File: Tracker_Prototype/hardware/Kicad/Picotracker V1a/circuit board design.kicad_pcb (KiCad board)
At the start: 2 copper layers, 31 x 20.1 mm, 27 parts, among them J1 Conn_01x06, J2 GND, J3 3.3V, J4 Unconnected, U1 MAX-M8C, U3 CMWX1ZZABZ-078, U6 MS5607-02BA

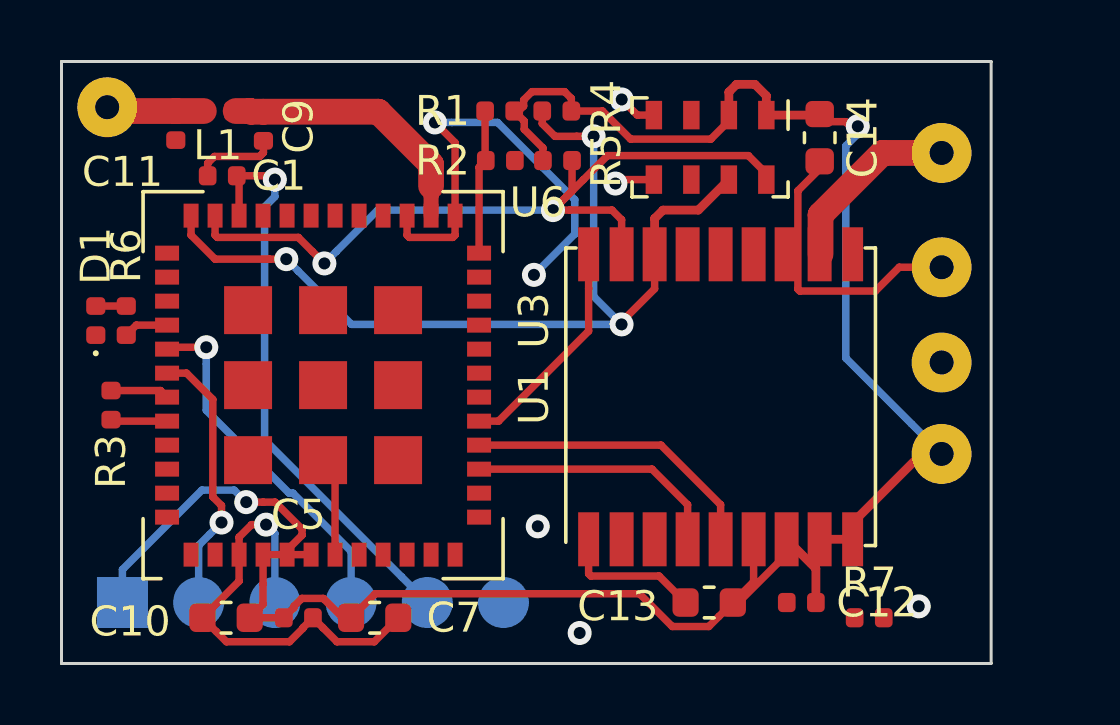
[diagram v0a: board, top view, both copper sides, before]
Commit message: added the switch. reorganised the prototype folder to have a "a" variant
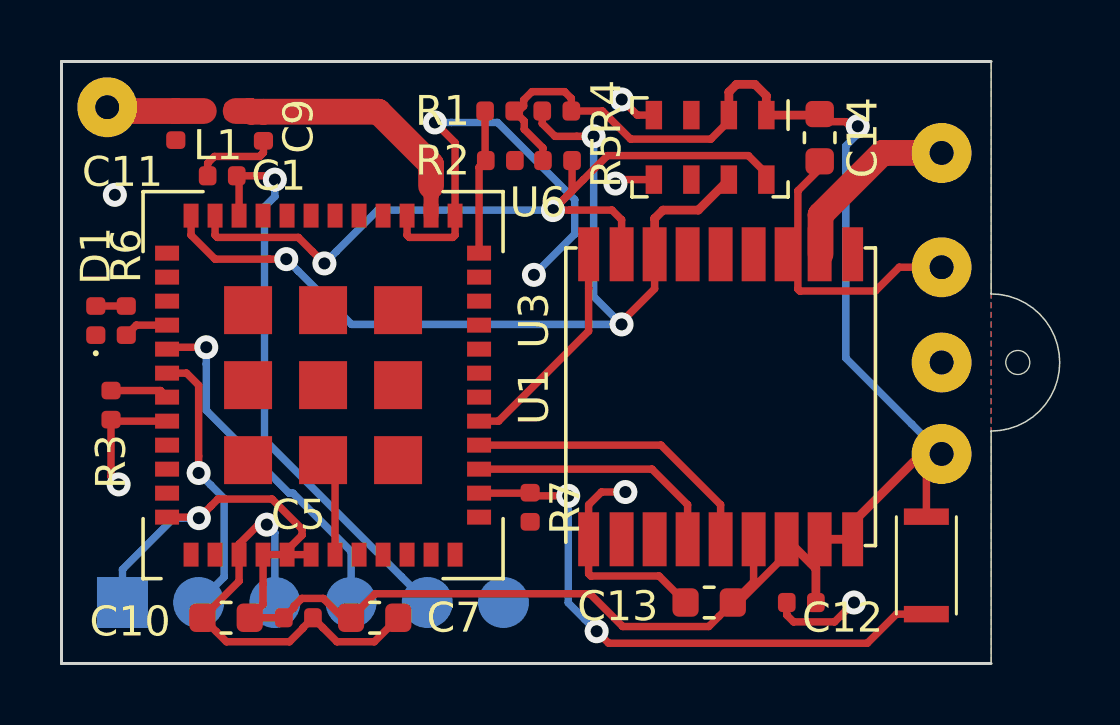
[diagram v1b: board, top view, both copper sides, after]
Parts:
- added J5: Unconnected, Connector_Wire:SolderWirePad_1x01_Drill0.8mm, F.Cu at (298.6, 170.1)
- added SW1: SW_Push, flight-computer:EVPAWCD4A, F.Cu at (295.5, 177.3)
- moved R7 11.9 mm to (282.3, 174.9), turned to 270 degrees
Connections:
- J1 pad 6: Net-(J1-Pad6) -> (no net)
- J4 pad 1: Net-(J4-Pad1) -> (no net)
- U1 pad 14: Net-(U1-Pad14) -> (no net)
- U1 pad 15: Net-(U1-Pad15) -> (no net)
- U1 pad 2: Net-(U1-Pad2) -> (no net)
- U1 pad 3: Net-(U1-Pad3) -> (no net)
- U3 pad 1: Net-(U3-Pad1) -> (no net)
- U3 pad 10: Net-(U3-Pad10) -> (no net)
- U3 pad 11: Net-(U3-Pad11) -> (no net)
- U3 pad 12: Net-(U3-Pad12) -> (no net)
- U3 pad 13: Net-(U3-Pad13) -> (no net)
- U3 pad 18: Net-(U3-Pad18) -> (no net)
- U3 pad 19: Net-(U3-Pad19) -> (no net)
- U3 pad 2: Net-(U3-Pad2) -> (no net)
- U3 pad 20: Net-(U3-Pad20) -> (no net)
- U3 pad 21: Net-(U3-Pad21) -> (no net)
- U3 pad 22: Net-(U3-Pad22) -> (no net)
- U3 pad 23: Net-(U3-Pad23) -> (no net)
- U3 pad 28: Net-(U3-Pad28) -> (no net)
- U3 pad 29: Net-(U3-Pad29) -> (no net)
- U3 pad 30: Net-(U3-Pad30) -> (no net)
- U3 pad 31: Net-(U3-Pad31) -> (no net)
- U3 pad 32: Net-(U3-Pad32) -> (no net)
- U3 pad 33: Net-(U3-Pad33) -> (no net)
- U3 pad 37: Net-(U3-Pad37) -> (no net)
- U3 pad 38: Net-(U3-Pad38) -> (no net)
- U3 pad 39: /VDD_TCXO -> (no net)
- U3 pad 45: Net-(U3-Pad45) -> (no net)
- U3 pad 46: Net-(U3-Pad46) -> (no net)
- U3 pad 47: Net-(U3-Pad47) -> (no net)
- U3 pad 48: /VDD_TCXO -> +3V3
- U3 pad 8: Net-(U3-Pad8) -> (no net)
- U3 pad 9: Net-(U3-Pad9) -> (no net)
- U6 pad 6: Net-(U6-Pad6) -> (no net)
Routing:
- net /SWITCH: track 0.00 -> 19.5 mm, vias 0 -> 2
- net GND: track 55.2 -> 62.9 mm, vias 7 -> 9
- net +3V3: track 76.4 -> 79.5 mm
- net (no net): vias 1 -> 0
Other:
- board size 31 x 20.1 mm -> 33.3 x 20.1 mm
